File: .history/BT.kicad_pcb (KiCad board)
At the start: 4 copper layers, 55 x 40 mm, 95 parts, among them J1 61300511121, J2 Conn_01x03_Pin, J3 S6B-PH-K-S, J4 Boxed_Header_02x03_SMT, K1 AGQ200A12Z, Q1 BSS123, U1 PCM5100A, U2 ESP32-WROOM-32U, U3 TLV4888DR, U4 TLVM23615RDNR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

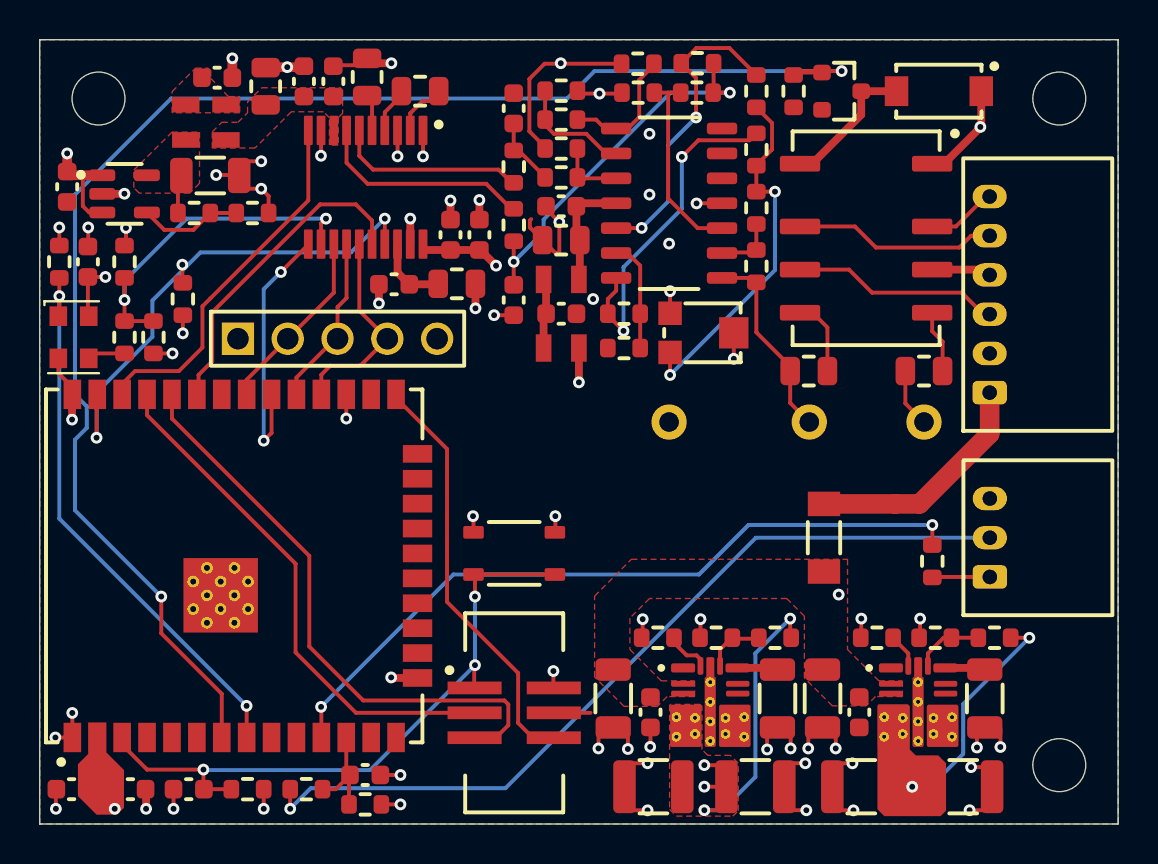
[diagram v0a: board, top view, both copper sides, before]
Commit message: added teardrops
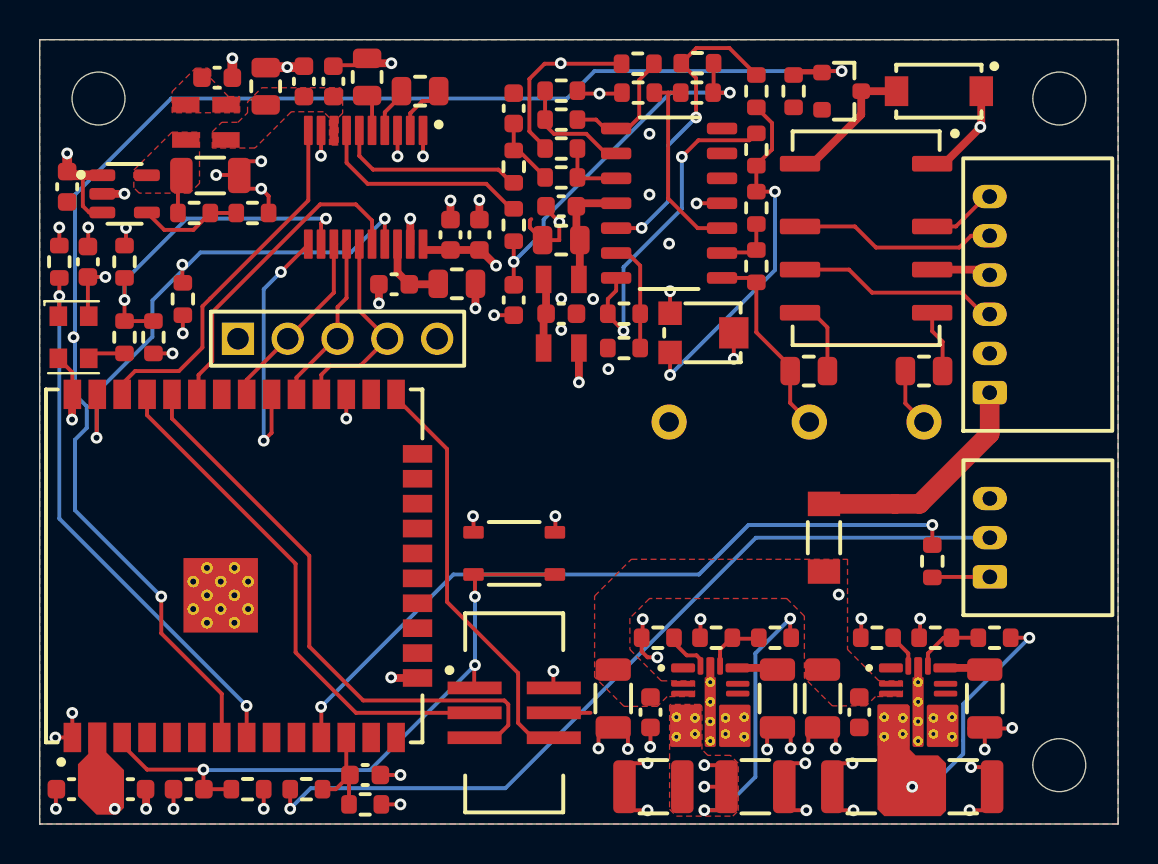
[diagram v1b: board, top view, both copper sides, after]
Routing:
- net GND: track 73.0 -> 73.2 mm, vias 58 -> 62
- net /SW_TO_BT_AUDIO: vias 2 -> 3
